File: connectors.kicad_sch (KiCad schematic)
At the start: 3 parts, among them J3 0430450200, J4 0436500200, J5 IPS1-110-01-L-D

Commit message: PCB[Silkscreen, DRC]: Though all drc erros minus one, not an issue just need to clear. Added silk logos
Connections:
- net COMH.N: now also J3.1; no longer J3.2
- net COMH.P: now also J3.2; no longer J3.1
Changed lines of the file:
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@@
+	(wire
+		(pts
+			(xy 101.6 78.74) (xy 111.76 78.74)
+		)
+		(stroke
+			(width 0)
+			(type default)
+		)
+	)
 	(wire
 		(pts
@@
 		)
 	)
+	(wire
+		(pts
+			(xy 101.6 73.66) (xy 111.76 73.66)
+		)
+		(stroke
+			(width 0)
+			(type default)
+		)
+	)
 	(bus
 		(pts
@@
 	(wire
 		(pts
+			(xy 160.02 87.63) (xy 168.91 87.63)
+		)
+		(stroke
+			(width 0)
+			(type default)
+		)
+	)
+	(wire
+		(pts
+			(xy 101.6 88.9) (xy 111.76 88.9)
+		)
+		(stroke
+			(width 0)
+			(type default)
+		)
+	)
+	(wire
+		(pts
+			(xy 152.4 77.47) (xy 168.91 77.47)
+		)
+		(stroke
+			(width 0)
+			(type default)
+		)
+	)
+	(bus
+		(pts
+			(xy 91.44 68.58) (xy 96.52 68.58)
+		)
+		(stroke
+			(width 0)
+			(type default)
+		)
+	)
+	(bus
+		(pts
+			(xy 203.2 71.12) (xy 203.2 77.47)
+		)
+		(stroke
+			(width 0)
+			(type default)
+		)
+	)
+	(wire
+		(pts
+			(xy 194.31 82.55) (xy 200.66 82.55)
+		)
+		(stroke
+			(width 0)
+			(type default)
+		)
+	)
+	(wire
+		(pts
+			(xy 194.31 80.01) (xy 200.66 80.01)
+		)
+		(stroke
+			(width 0)
+			(type default)
+		)
+	)
+	(bus
+		(pts
+			(xy 207.01 66.04) (xy 203.2 71.12)
+		)
+		(stroke
+			(width 0)
+			(type default)
+		)
+	)
+	(wire
+		(pts
+			(xy 160.02 92.71) (xy 168.91 92.71)
+		)
+		(stroke
+			(width 0)
+			(type default)
+		)
+	)
+	(wire
+		(pts
 			(xy 101.6 93.98) (xy 111.76 93.98)
 		)
@@
 	(wire
 		(pts
-			(xy 160.02 87.63) (xy 168.91 87.63)
-		)
-		(stroke
-			(width 0)
-			(type default)
-		)
-	)
-	(wire
-		(pts
-			(xy 152.4 77.47) (xy 168.91 77.47)
-		)
-		(stroke
-			(width 0)
-			(type default)
-		)
-	)
-	(bus
-		(pts
-			(xy 91.44 68.58) (xy 96.52 68.58)
-		)
-		(stroke
-			(width 0)
-			(type default)
-		)
-	)
-	(bus
-		(pts
-			(xy 203.2 71.12) (xy 203.2 77.47)
-		)
-		(stroke
-			(width 0)
-			(type default)
-		)
-	)
-	(wire
-		(pts
-			(xy 194.31 82.55) (xy 200.66 82.55)
-		)
-		(stroke
-			(width 0)
-			(type default)
-		)
-	)
-	(wire
-		(pts
-			(xy 194.31 80.01) (xy 200.66 80.01)
-		)
-		(stroke
-			(width 0)
-			(type default)
-		)
-	)
-	(bus
-		(pts
-			(xy 207.01 66.04) (xy 203.2 71.12)
-		)
-		(stroke
-			(width 0)
-			(type default)
-		)
-	)
-	(wire
-		(pts
-			(xy 160.02 92.71) (xy 168.91 92.71)
-		)
-		(stroke
-			(width 0)
-			(type default)
-		)
-	)
-	(wire
-		(pts
 			(xy 210.82 99.06) (xy 210.82 100.33)
 		)
@@
 	(wire
 		(pts
-			(xy 101.6 78.74) (xy 111.76 78.74)
-		)
-		(stroke
-			(width 0)
-			(type default)
-		)
-	)
-	(wire
-		(pts
 			(xy 66.04 78.74) (xy 66.04 81.28)
 		)
@@
 		(pts
 			(xy 203.2 77.47) (xy 203.2 80.01)
-		)
-		(stroke
-			(width 0)
-			(type default)
-		)
-	)
-	(wire
-		(pts
-			(xy 101.6 88.9) (xy 111.76 88.9)
-		)
-		(stroke
-			(width 0)
-			(type default)
-		)
-	)
-	(wire
-		(pts
-			(xy 101.6 73.66) (xy 111.76 73.66)
 		)
 		(stroke
@@
 		)
 	)
+	(label "COML.P"
+		(at 102.87 78.74 0)
+		(effects
+			(font
+				(size 1.27 1.27)
+			)
+			(justify left bottom)
+		)
+	)
 	(label "TAP8"
 		(at 163.83 100.33 0)
@@
 		)
 	)
-	(label "COMH.N"
-		(at 102.87 93.98 0)
-		(effects
-			(font
-				(size 1.27 1.27)
-			)
-			(justify left bottom)
-		)
-	)
 	(label "T_P7"
 		(at 200.66 95.25 180)
@@
 		)
 	)
+	(label "COMH.P"
+		(at 102.87 93.98 0)
+		(effects
+			(font
+				(size 1.27 1.27)
+			)
+			(justify left bottom)
+		)
+	)
 	(label "TAP0"
 		(at 163.83 80.01 0)
@@
 		)
 	)
-	(label "COMH.P"
-		(at 102.87 88.9 0)
-		(effects
-			(font
-				(size 1.27 1.27)
-			)
-			(justify left bottom)
-		)
-	)
 	(label "TAP1"
 		(at 163.83 82.55 0)
@@
 		)
 	)
-	(label "COML.P"
-		(at 102.87 73.66 0)
+	(label "COMH.N"
+		(at 102.87 88.9 0)
 		(effects
 			(font
@@
 		)
 	)
-	(label "COML.N"
-		(at 102.87 78.74 0)
-		(effects
-			(font
-				(size 1.27 1.27)
-			)
-			(justify left bottom)
-		)
-	)
 	(label "T_P2"
 		(at 200.66 82.55 180)
@@
 			)
 			(justify right bottom)
+		)
+	)
+	(label "COML.N"
+		(at 102.87 73.66 0)
+		(effects
+			(font
+				(size 1.27 1.27)
+			)
+			(justify left bottom)
 		)
 	)
@@
 	(symbol
 		(lib_id "remote_0436500200:0436500200")
-		(at 111.76 78.74 0)
-		(mirror x)
+		(at 111.76 73.66 0)
 		(unit 1)
 		(body_style 0)
@@
 		(dnp no)
 		(property "Reference" "J4"
+			(at 114.3 82.55 0)
+			(show_name no)
+			(do_not_autoplace no)
+			(effects
+				(font
+					(size 1.27 1.27)
+				)
+				(justify left)
+			)
+		)
+		(property "Value" "0436500200"
 			(at 114.3 69.85 0)
 			(show_name no)
@@
 			)
 		)
-		(property "Value" "0436500200"
-			(at 114.3 82.55 0)
-			(show_name no)
-			(do_not_autoplace no)
-			(effects
-				(font
-					(size 1.27 1.27)
-				)
-				(justify left)
-			)
-		)
 		(property "Footprint" "remote_0436500200:CONN_SD-43650-001_02_MOL"
-			(at 111.76 78.74 0)
+			(at 111.76 73.66 0)
 			(hide yes)
 			(show_name no)
@@
 		)
 		(property "Datasheet" "https://www.molex.com/content/dam/molex/molex-dot-com/products/automated/en-us/salesdrawingpdf/436/43650/436500200_sd.pdf?inline"
-			(at 111.76 78.74 0)
+			(at 111.76 73.66 0)
 			(hide yes)
 			(show_name no)
@@
 		)
 		(property "Description" "Connector Header Through Hole, Right Angle 2 position 0.118\" (3.00mm)"
-			(at 111.76 78.74 0)
+			(at 111.76 73.66 0)
 			(hide yes)
 			(show_name no)
@@
 		)
 		(property "Manufacturer" "Molex"
-			(at 111.76 78.74 0)
+			(at 111.76 73.66 0)
 			(hide yes)
 			(show_name no)
@@
 		)
 		(property "Manufacturer Part Number" "0436500200"
-			(at 111.76 78.74 0)
+			(at 111.76 73.66 0)
 			(hide yes)
 			(show_name no)
@@
 		)
 		(property "Vendor" ""
-			(at 111.76 78.74 0)
+			(at 111.76 73.66 0)
 			(hide yes)
 			(show_name no)
@@
 		)
 		(property "Vendor Part Number" ""
-			(at 111.76 78.74 0)
+			(at 111.76 73.66 0)
 			(hide yes)
 			(show_name no)
@@
 		)
 		(property "Mass (g)" ""
-			(at 111.76 78.74 0)
+			(at 111.76 73.66 0)
 			(hide yes)
 			(show_name no)
@@
 		)
 		(property "RQjC (C/W)" ""
-			(at 111.76 78.74 0)
+			(at 111.76 73.66 0)
 			(hide yes)
 			(show_name no)
@@
 		)
 		(property "RQjC_top (C/W)" ""
-			(at 111.76 78.74 0)
+			(at 111.76 73.66 0)
 			(hide yes)
 			(show_name no)
@@
 		)
 		(property "Temp_max (C)" ""
-			(at 111.76 78.74 0)
+			(at 111.76 73.66 0)
 			(hide yes)
 			(show_name no)
@@
 		)
 		(property "Temp_min (C)" ""
-			(at 111.76 78.74 0)
+			(at 111.76 73.66 0)
 			(hide yes)
 			(show_name no)
@@
 		)
 		(property "Power Dissipation (W)" ""
-			(at 111.76 78.74 0)
+			(at 111.76 73.66 0)
 			(hide yes)
 			(show_name no)
@@
 		)
 		(property "Rate" ""
-			(at 111.76 78.74 0)
+			(at 111.76 73.66 0)
 			(hide yes)
 			(show_name no)
@@
 		)
 		(property "SAP Code" ""
-			(at 111.76 78.74 0)
-			(hide yes)
-			(show_name no)
+			(at 111.76 73.66 0)
+			(hide yes)
+			(show_name no)

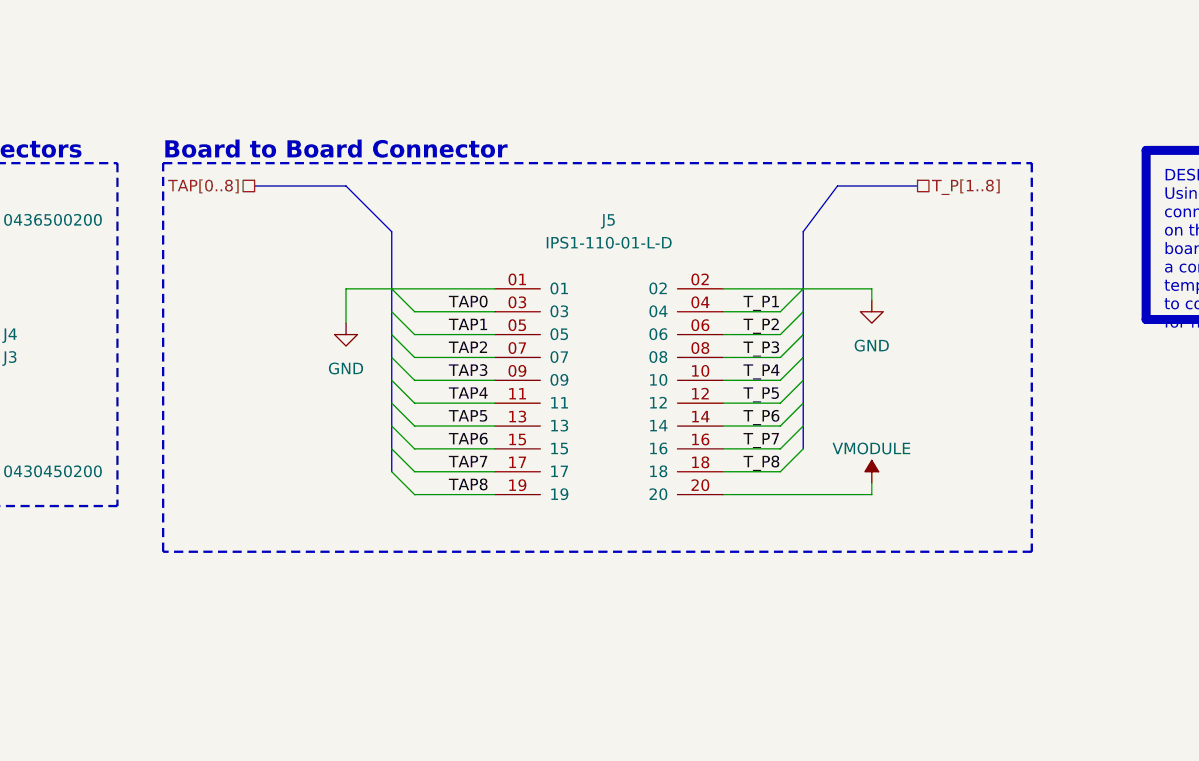
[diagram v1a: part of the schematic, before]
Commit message: PCB[Mounting]: Messing with mounting holes for board to board connection. SCH[Naming]: Small naming changes, T_P -> TMP
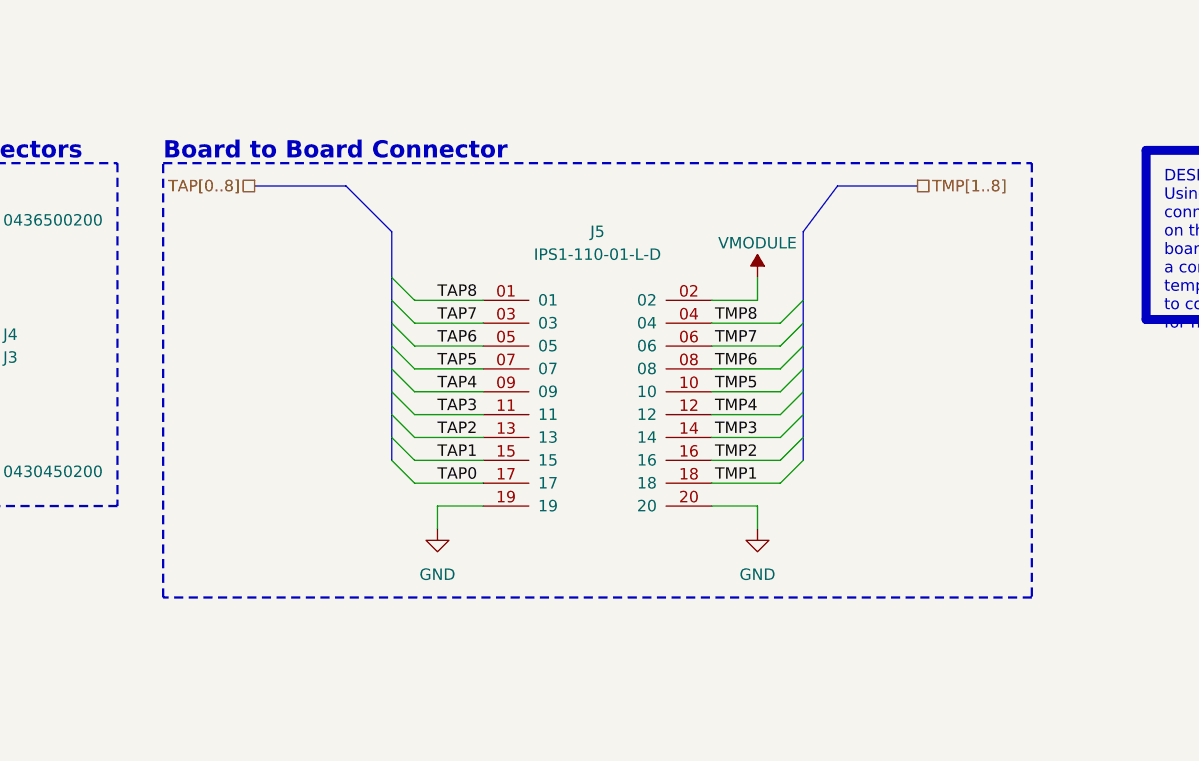
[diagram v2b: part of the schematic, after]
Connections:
- net GND: now also J5.19, J5.20; no longer J5.01, J5.02
- net TAP0: now also J5.17; no longer J5.03
- net TAP1: now also J5.15; no longer J5.05
- net TAP2: now also J5.13; no longer J5.07
- net TAP3: now also J5.11; no longer J5.09
- net TAP4: now also J5.09; no longer J5.11
- net TAP5: now also J5.07; no longer J5.13
- net TAP6: now also J5.05; no longer J5.15
- net TAP7: now also J5.03; no longer J5.17
- net TAP8: now also J5.01; no longer J5.19
- net VMODULE: now also J5.02; no longer J5.20
- net T_P1 renamed TMP8
- net T_P2 renamed TMP7
- net T_P3 renamed TMP6
- net T_P4 renamed TMP5
- net T_P5 renamed TMP4
- net T_P6 renamed TMP3
- net T_P7 renamed TMP2
- net T_P8 renamed TMP1
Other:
- moved on the sheet: J5

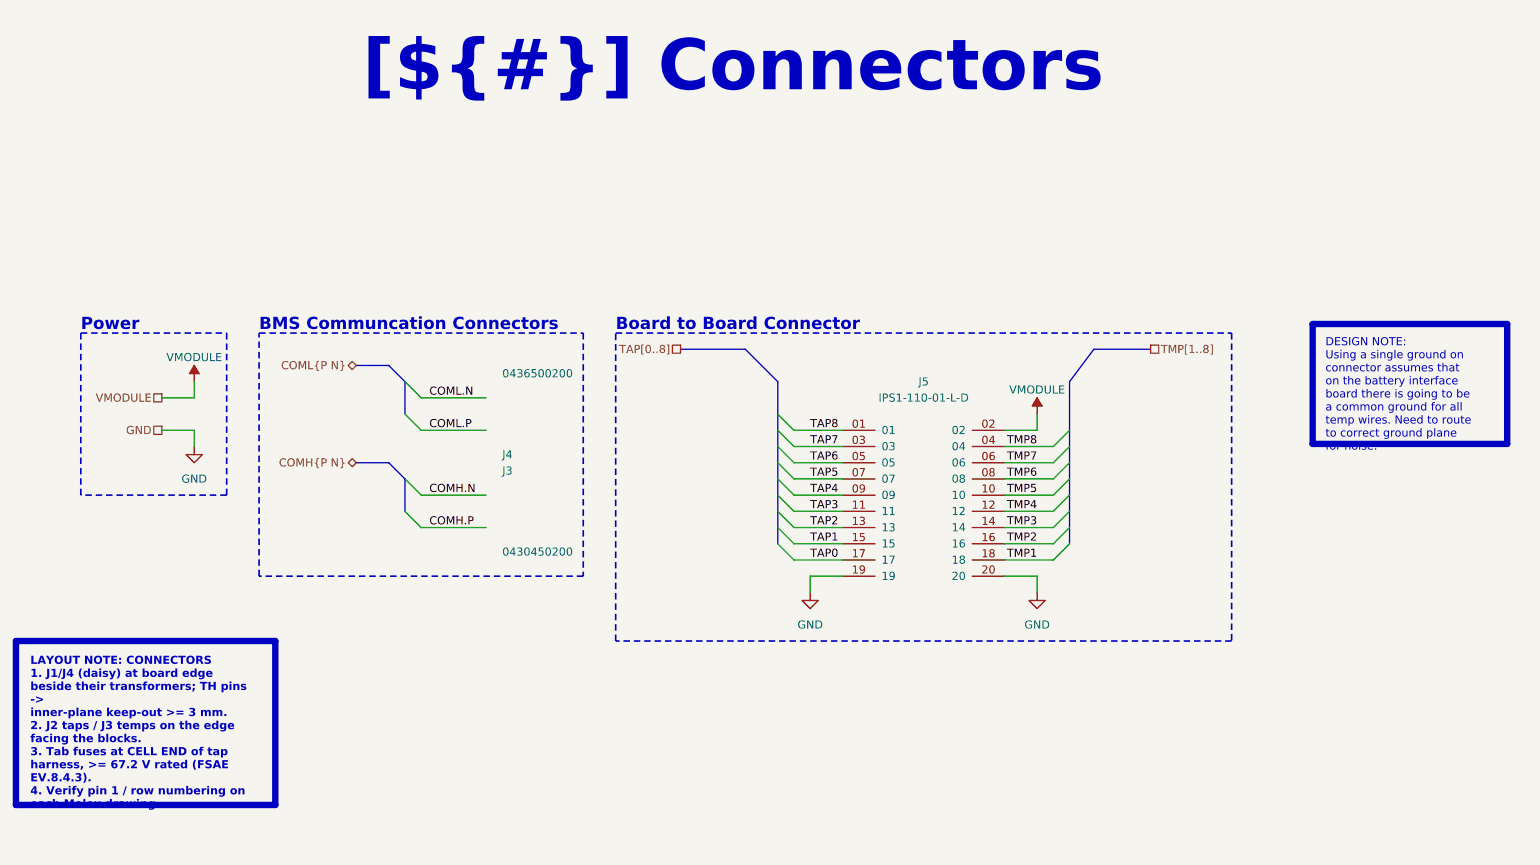
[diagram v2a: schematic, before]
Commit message: PCB[Grounding, Heat]: Added some more pours for heat considerations for bjt, stiched more vias for heat consideration on balanace resistors. SCH[Notes, Block Diagram]: Working on spelling and notes updates, started block diagram.
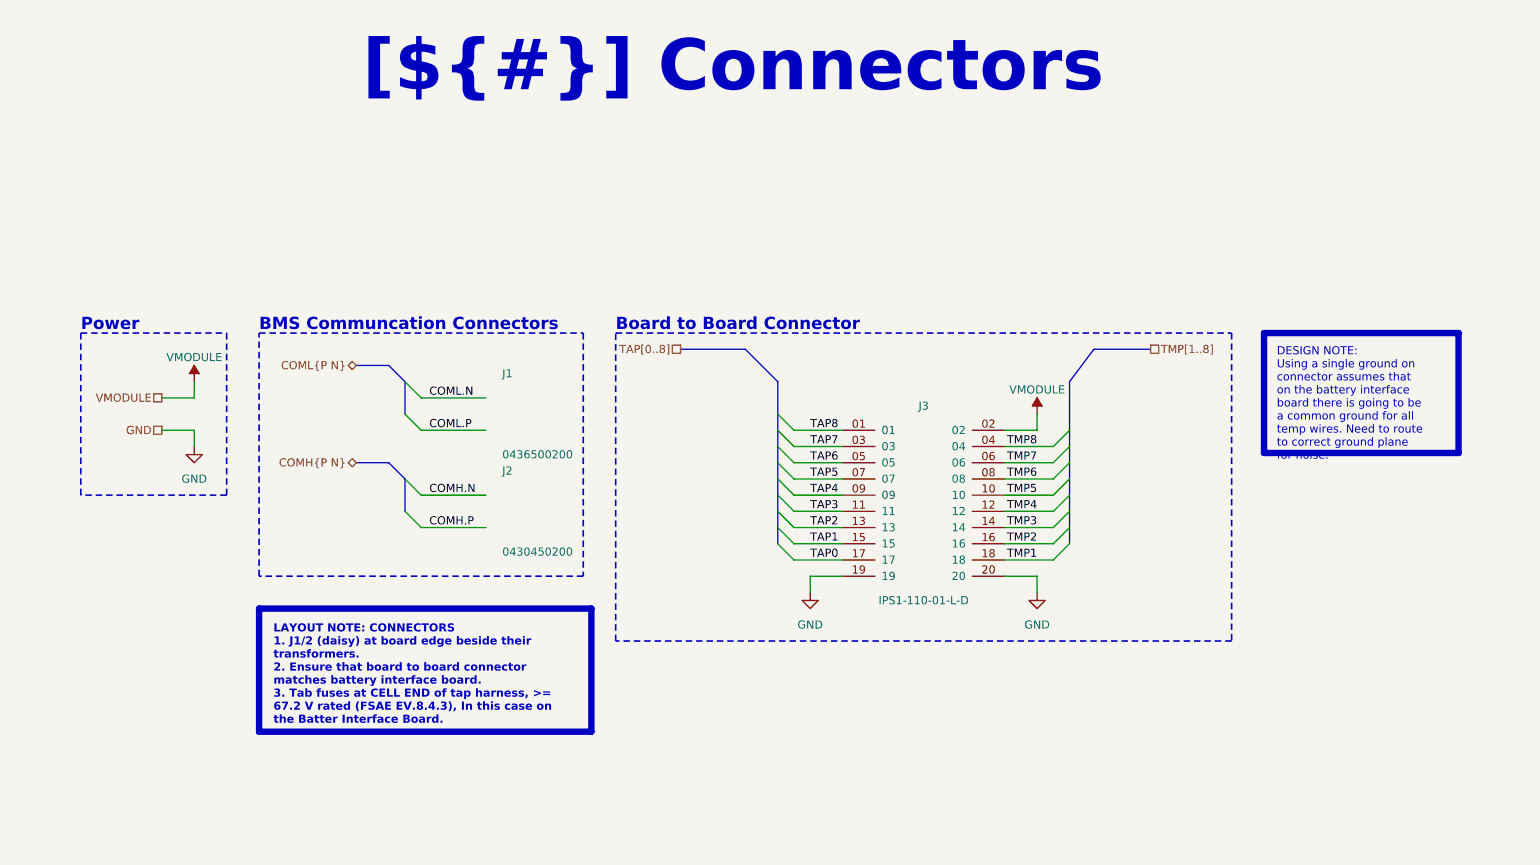
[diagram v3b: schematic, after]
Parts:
- renumbered J4 to J1, J3 to J2, J5 to J3
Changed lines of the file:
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@@
 		)
 	)
-	(text_box "LAYOUT NOTE: CONNECTORS\n1. J1/J4 (daisy) at board edge beside their transformers; TH pins ->\n   inner-plane keep-out >= 3 mm.\n2. J2 taps / J3 temps on the edge facing the blocks.\n3. Tab fuses at CELL END of tap harness, >= 67.2 V rated (FSAE EV.8.4.3).\n4. Verify pin 1 / row numbering on each Molex drawing."
+	(text_box "LAYOUT NOTE: CONNECTORS\n1. J1/2 (daisy) at board edge beside their transformers.\n2. Ensure that board to board connector matches battery interface board.\n3. Tab fuses at CELL END of tap harness, >= 67.2 V rated (FSAE EV.8.4.3), In this case on the Batter Interface Board."
 		(exclude_from_sim no)
-		(at 38.1 111.76 0)
-		(size 40.64 25.6924)
+		(at 76.2 106.68 0)
+		(size 52.07 19.2916)
 		(margins 2.25 2.25 2.25 2.25)
 		(stroke
@@
 	(text_box "DESIGN NOTE:\nUsing a single ground on connector assumes that on the battery interface board there is going to be a common ground for all temp wires. Need to route to correct ground plane for noise."
 		(exclude_from_sim no)
-		(at 241.3 62.082 0)
+		(at 233.68 63.5 0)
 		(size 30.48 18.7916)
 		(margins 2 2 2 2)
@@
 		(in_pos_files yes)
 		(dnp no)
-		(property "Reference" "J4"
+		(property "Reference" "J1"
+			(at 114.3 69.85 0)
+			(show_name no)
+			(do_not_autoplace no)
+			(effects
+				(font
+					(size 1.27 1.27)
+				)
+				(justify left)
+			)
+		)
+		(property "Value" "0436500200"
 			(at 114.3 82.55 0)
-			(show_name no)
-			(do_not_autoplace no)
-			(effects
-				(font
-					(size 1.27 1.27)
-				)
-				(justify left)
-			)
-		)
-		(property "Value" "0436500200"
-			(at 114.3 69.85 0)
 			(show_name no)
 			(do_not_autoplace no)
@@
 			(project "bms_slave"
 				(path "/f9e05184-c88b-4a88-ae9c-ab2bdb32be7c/c5103ceb-5325-4a84-a025-9638a412984e/6c6a059d-71c7-49d0-bb31-68bf0320ac4e"
-					(reference "J4")
+					(reference "J1")
 					(unit 1)
 				)
@@
 		(dnp no)
 		(fields_autoplaced yes)
-		(property "Reference" "#PWR09"
+		(property "Reference" "#PWR014"
 			(at 198.12 110.49 0)
 			(hide yes)
@@
 			(project "bms_slave"
 				(path "/f9e05184-c88b-4a88-ae9c-ab2bdb32be7c/c5103ceb-5325-4a84-a025-9638a412984e/6c6a059d-71c7-49d0-bb31-68bf0320ac4e"
-					(reference "#PWR09")
+					(reference "#PWR014")
 					(unit 1)
 				)
@@
 		(in_pos_files yes)
 		(dnp no)
-		(property "Reference" "J3"
+		(property "Reference" "J2"
 			(at 114.3 85.09 0)
 			(show_name no)
@@
 			(project "bms_slave"
 				(path "/f9e05184-c88b-4a88-ae9c-ab2bdb32be7c/c5103ceb-5325-4a84-a025-9638a412984e/6c6a059d-71c7-49d0-bb31-68bf0320ac4e"
-					(reference "J3")
+					(reference "J2")
 					(unit 1)
 				)
@@
 		(in_pos_files yes)
 		(dnp no)
-		(property "Reference" "#PWR053"
+		(property "Reference" "#PWR010"
 			(at 66.04 74.93 0)
 			(hide yes)
@@
 			(project "bms_slave"
 				(path "/f9e05184-c88b-4a88-ae9c-ab2bdb32be7c/c5103ceb-5325-4a84-a025-9638a412984e/6c6a059d-71c7-49d0-bb31-68bf0320ac4e"
-					(reference "#PWR053")
+					(reference "#PWR010")
 					(unit 1)
 				)
@@
 		(in_pos_files yes)
 		(dnp no)
-		(fields_autoplaced yes)
-		(property "Reference" "J5"
-			(at 180.34 71.12 0)
+		(property "Reference" "J3"
+			(at 180.34 74.93 0)
 			(show_name no)
 			(do_not_autoplace no)
@@
 		)
 		(property "Value" "IPS1-110-01-L-D"
-			(at 180.34 73.66 0)
+			(at 180.34 105.41 0)
 			(show_name no)
 			(do_not_autoplace no)
@@
 			(project "bms_slave"
 				(path "/f9e05184-c88b-4a88-ae9c-ab2bdb32be7c/c5103ceb-5325-4a84-a025-9638a412984e/6c6a059d-71c7-49d0-bb31-68bf0320ac4e"
-					(reference "J5")
+					(reference "J3")
 					(unit 1)
 				)
@@
 		(dnp no)
 		(fields_autoplaced yes)
-		(property "Reference" "#PWR08"
+		(property "Reference" "#PWR011"
 			(at 66.04 87.63 0)
 			(hide yes)
@@
 			(project "bms_slave"
 				(path "/f9e05184-c88b-4a88-ae9c-ab2bdb32be7c/c5103ceb-5325-4a84-a025-9638a412984e/6c6a059d-71c7-49d0-bb31-68bf0320ac4e"
-					(reference "#PWR08")
+					(reference "#PWR011")
 					(unit 1)
 				)
@@
 		(in_pos_files yes)
 		(dnp no)
-		(property "Reference" "#PWR058"
+		(property "Reference" "#PWR013"
 			(at 198.12 80.01 0)
 			(hide yes)
@@
 			(project "bms_slave"
 				(path "/f9e05184-c88b-4a88-ae9c-ab2bdb32be7c/c5103ceb-5325-4a84-a025-9638a412984e/6c6a059d-71c7-49d0-bb31-68bf0320ac4e"
-					(reference "#PWR058")
+					(reference "#PWR013")
 					(unit 1)
 				)
@@
 		(dnp no)
 		(fields_autoplaced yes)
-		(property "Reference" "#PWR057"
+		(property "Reference" "#PWR012"
 			(at 162.56 110.49 0)
 			(hide yes)
@@
 			(project "bms_slave"
 				(path "/f9e05184-c88b-4a88-ae9c-ab2bdb32be7c/c5103ceb-5325-4a84-a025-9638a412984e/6c6a059d-71c7-49d0-bb31-68bf0320ac4e"
-					(reference "#PWR057")
+					(reference "#PWR012")
 					(unit 1)
 				)
